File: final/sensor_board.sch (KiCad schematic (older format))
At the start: 73 parts, among them J2 USB_microB_2040002-1, J3 Arduino_ICSP, J4 Conn_01x02_Male, J5 Conn_01x15_Male, J6 Conn_01x15_Male, J7 BT CONFIG, SW1 SW_DIP_x01, U10 BQ24075, U11 BQ27441-G1, U2 TXS0104E, U3 MCP1702T-3302E/CBCT-ND, U4 FT232RL, U5 RN4871, U6 MCP1702T-5002E_CB, U7 TPS2113ADRBR, U8 US5881, U9 ATMEGA328PB-ANR, Y1 16MHz

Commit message: Linear Regulator -> Boost DC-DC
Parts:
- removed C13: 10µF, Capacitor_SMD:C_0805_2012Metric, symbol Device:C
- removed C19: 10µF, Capacitor_SMD:C_0603_1608Metric, symbol Device:C
- removed C8, C9: 1µF, Capacitor_SMD:C_0603_1608Metric, symbol Device:C
- removed J4: Conn_01x02_Male, symbol Connector:Conn_01x02_Male
- removed R12, R19: 1K, Resistor_SMD:R_0603_1608Metric, symbol Device:R
- removed R13: 100k, Resistor_SMD:R_0603_1608Metric, symbol Device:R
- removed R24: 10k, Resistor_SMD:R_0603_1608Metric, symbol Device:R
- removed U5: RN4871, RF_Module:Microchip_RN4871, symbol RF_Bluetooth:RN4871
- removed U6: MCP1702T-5002E_CB, Package_TO_SOT_SMD:SOT-23, symbol sensor_board-rescue:MCP1702T-5002E_CB-final
- added C10: 0.1µF, Capacitor_SMD:C_0603_1608Metric, symbol Device:C
- added C11, C20, C5: 10µF, Capacitor_SMD:C_0603_1608Metric, symbol Device:C
- added C15: 10µF, Capacitor_SMD:C_0805_2012Metric, symbol Device:C
- added J3: Conn_01x02_Male, symbol Connector:Conn_01x02_Male
- added L1: 4.7uH, symbol pspice:INDUCTOR
- added R14, R21: 1K, Resistor_SMD:R_0603_1608Metric, symbol Device:R
- added R15: 100k, Resistor_SMD:R_0603_1608Metric, symbol Device:R
- added R2: 2M, Resistor_SMD:R_0603_1608Metric, symbol Device:R
- added R23: 10k, Resistor_SMD:R_0603_1608Metric, symbol Device:R
- added R3: 220K, Resistor_SMD:R_0603_1608Metric, symbol Device:R
- added U4: TPS61200DRC, Package_SON:Texas_S-PVSON-N10_ThermalVias, symbol Regulator_Switching:TPS61200DRC
- added U6: RN4871, RF_Module:Microchip_RN4871, symbol RF_Bluetooth:RN4871
- U1: renamed from U?; symbol final:NC7SZ04P5X -> sensor_board-rescue:NC7SZ04P5X-final
- gave numbers to parts that had none: 1
- renumbered C10 to C12, C11 to C13, C12 to C14, C14 to C16, C15 to C17, C16 to C18, C17 to C19, C18 to C21, C20 to C22, C21 to C23, C1 to C3, C7 to C4, C3 to C6, C4 to C7, C5 to C8, C6 to C9, J2 to J1, J3 to J2, J5 to J4, J6 to J5, J7 to J6, R8 to R10, R9 to R11, R10 to R12, R11 to R13, R14 to R16, R15 to R17, R16 to R18, R17 to R19, R18 to R20, R20 to R22, R21 to R24, R22 to R25, R23 to R26, R2 to R4, R3 to R5, R4 to R6, R5 to R7, R6 to R8, R7 to R9, U3 to U2, U2 to U3, U4 to U5
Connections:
- wire segments 230 -> 252
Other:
- moved on the sheet: C1, C12, C13, C14, C16, C17, C18, C19, C2, C21, C22, C23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

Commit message: Footprint assignment
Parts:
- R1, R11, R5: footprint (none) -> Resistor_SMD:R_0603_1608Metric
- U5: footprint (none) -> mp3b:FT232RQ
- U8: footprint (none) -> mp3b:TSOT-3L
- U9: footprint (none) -> mp3b:Atmega328pb
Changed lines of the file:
@@
 EESchema Schematic File Version 4
 LIBS:sensor_board-cache
-LIBS:main_board-cache
-EELAYER 26 0
+EELAYER 29 0
 EELAYER END
 $Descr User 18504 11811
@@
 F 0 "U9" H 10450 8515 50  0000 C CNN
 F 1 "ATMEGA328PB-ANR" H 10450 8424 50  0000 C CNN
-F 2 "" H 10450 6150 50  0001 C CNN
+F 2 "mp3b:Atmega328pb" H 10450 6150 50  0001 C CNN
 F 3 "" H 10450 6150 50  0001 C CNN
 	1    10450 6350
@@
 F 0 "U5" H 5150 7315 50  0000 C CNN
 F 1 "FT232RL" H 5150 7224 50  0000 C CNN
-F 2 "" H 5150 6700 50  0001 C CNN
+F 2 "mp3b:FT232RQ" H 5150 6700 50  0001 C CNN
 F 3 "" H 5150 6700 50  0001 C CNN
 	1    5150 5750
@@
 F 0 "R5" H 6720 9486 50  0000 L CNN
 F 1 "1K" H 6720 9395 50  0000 L CNN
-F 2 "" V 6580 9440 50  0001 C CNN
+F 2 "Resistor_SMD:R_0603_1608Metric" V 6580 9440 50  0001 C CNN
 F 3 "~" H 6650 9440 50  0001 C CNN
 	1    6650 9440
@@
 F 0 "R11" H 7430 9196 50  0000 L CNN
 F 1 "1K" H 7430 9105 50  0000 L CNN
-F 2 "" V 7290 9150 50  0001 C CNN
+F 2 "Resistor_SMD:R_0603_1608Metric" V 7290 9150 50  0001 C CNN
 F 3 "~" H 7360 9150 50  0001 C CNN
 	1    7360 9150
@@
 F 0 "R1" H 2850 9516 50  0000 L CNN
 F 1 "47K" H 2850 9425 50  0000 L CNN
-F 2 "" V 2710 9470 50  0001 C CNN
+F 2 "Resistor_SMD:R_0603_1608Metric" V 2710 9470 50  0001 C CNN
 F 3 "~" H 2780 9470 50  0001 C CNN
 	1    2780 9470
@@
 F 0 "U8" H 9100 9735 50  0000 C CNN
 F 1 "US5881" H 9100 9644 50  0000 C CNN
-F 2 "" H 9100 9370 50  0001 C CNN
+F 2 "mp3b:TSOT-3L" H 9100 9370 50  0001 C CNN
 F 3 "" H 9100 9370 50  0001 C CNN
 	1    9100 9370

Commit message: Footprint Assigned
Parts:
- J3: footprint (none) -> Connector_PinHeader_2.54mm:PinHeader_1x02_P2.54mm_Vertical_SMD_Pin1Right
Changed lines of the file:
@@
 F 0 "J3" H 16823 4280 50  0000 R CNN
 F 1 "Conn_01x02_Male" H 16823 4371 50  0000 R CNN
-F 2 "" H 16850 4400 50  0001 C CNN
+F 2 "Connector_PinHeader_2.54mm:PinHeader_1x02_P2.54mm_Vertical_SMD_Pin1Right" H 16850 4400 50  0001 C CNN
 F 3 "~" H 16850 4400 50  0001 C CNN
 	1    16850 4400

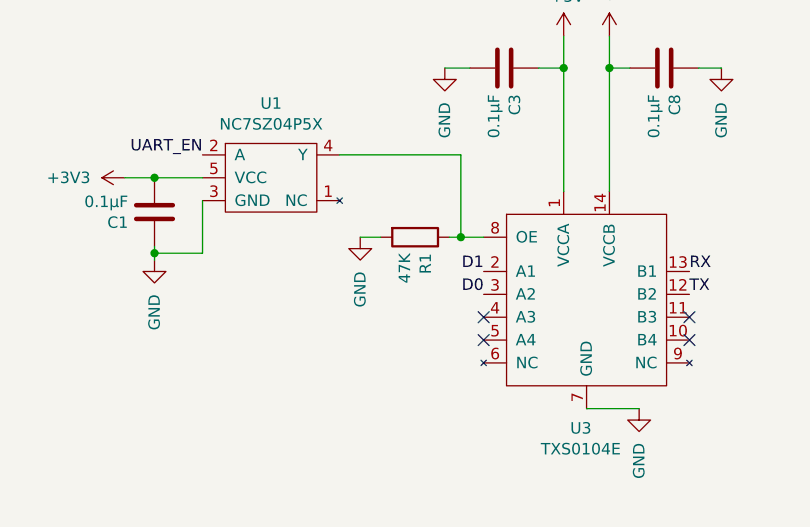
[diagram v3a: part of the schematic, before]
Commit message: Change pull up/down resistor values for logic level enable pins
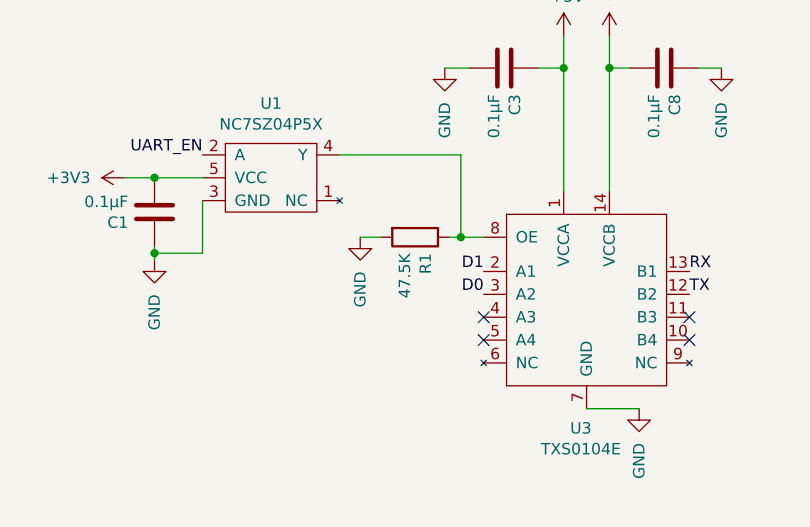
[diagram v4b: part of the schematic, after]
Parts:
- R1: value 47K -> 47.5K
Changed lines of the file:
@@
 EESchema Schematic File Version 4
 LIBS:sensor_board-cache
-EELAYER 29 0
+EELAYER 26 0
 EELAYER END
 $Descr User 18504 11811
@@
 P 2780 9470
 F 0 "R1" H 2850 9516 50  0000 L CNN
-F 1 "47K" H 2850 9425 50  0000 L CNN
+F 1 "47.5K" H 2850 9425 50  0000 L CNN
 F 2 "Resistor_SMD:R_0603_1608Metric" V 2710 9470 50  0001 C CNN
 F 3 "~" H 2780 9470 50  0001 C CNN
